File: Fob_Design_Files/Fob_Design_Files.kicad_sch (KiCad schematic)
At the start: 27 parts, among them IC2 TLV70030DDCT, U1 MAX16054AZT_T, U2 CC1101RGPR, U3 BU2032SM-JJ-GTR, U4 STM32C011F4Px, Y1 NX3225GA-26.000MHZ-EXS00A-CG0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

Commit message: Completed schematic
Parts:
- added J1: Conn_01x04_Pin, Connector_PinHeader_2.54mm:PinHeader_1x04_P2.54mm_Vertical, symbol Connector:Conn_01x04_Pin
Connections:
- net GND: now also J1.1 (Pin_1)
- net SWCLK: now also J1.2 (Pin_2)
- net SWDIO: now also J1.3 (Pin_3)
- net VDD: now also J1.4 (Pin_4)
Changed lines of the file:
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@@
 		)
 	)
+	(global_label "SWDIO"
+		(shape input)
+		(at 232.41 74.93 180)
+		(fields_autoplaced yes)
+		(effects
+			(font
+				(size 1.27 1.27)
+			)
+			(justify right)
+		)
+		(property "Intersheetrefs" "${INTERSHEET_REFS}"
+			(at 223.5586 74.93 0)
+			(effects
+				(font
+					(size 1.27 1.27)
+				)
+				(justify right)
+				(hide yes)
+			)
+		)
+	)
 	(global_label "RBIAS"
 		(shape input)
@@
 		)
 	)
+	(global_label "VDD"
+		(shape input)
+		(at 232.41 72.39 180)
+		(fields_autoplaced yes)
+		(effects
+			(font
+				(size 1.27 1.27)
+			)
+			(justify right)
+		)
+		(property "Intersheetrefs" "${INTERSHEET_REFS}"
+			(at 225.7962 72.39 0)
+			(effects
+				(font
+					(size 1.27 1.27)
+				)
+				(justify right)
+				(hide yes)
+			)
+		)
+	)
 	(global_label "SWDIO"
 		(shape input)
@@
 		)
 	)
+	(global_label "SWCLK"
+		(shape input)
+		(at 232.41 77.47 180)
+		(fields_autoplaced yes)
+		(effects
+			(font
+				(size 1.27 1.27)
+			)
+			(justify right)
+		)
+		(property "Intersheetrefs" "${INTERSHEET_REFS}"
+			(at 223.1958 77.47 0)
+			(effects
+				(font
+					(size 1.27 1.27)
+				)
+				(justify right)
+				(hide yes)
+			)
+		)
+	)
 	(symbol
 		(lib_id "SamacSys_Parts:BU2032SM-JJ-GTR")
@@
 	)
 	(symbol
+		(lib_id "Connector:Conn_01x04_Pin")
+		(at 237.49 77.47 180)
+		(unit 1)
+		(exclude_from_sim no)
+		(in_bom yes)
+		(on_board yes)
+		(dnp no)
+		(fields_autoplaced yes)
+		(property "Reference" "J1"
+			(at 238.76 74.9299 0)
+			(effects
+				(font
+					(size 1.27 1.27)
+				)
+				(justify right)
+			)
+		)
+		(property "Value" "Conn_01x04_Pin"
+			(at 238.76 77.4699 0)
+			(effects
+				(font
+					(size 1.27 1.27)
+				)
+				(justify right)
+			)
+		)
+		(property "Footprint" "Connector_PinHeader_2.54mm:PinHeader_1x04_P2.54mm_Vertical"
+			(at 237.49 77.47 0)
+			(effects
+				(font
+					(size 1.27 1.27)
+				)
+				(hide yes)
+			)
+		)
+		(property "Datasheet" "~"
+			(at 237.49 77.47 0)
+			(effects
+				(font
+					(size 1.27 1.27)
+				)
+				(hide yes)
+			)
+		)
+		(property "Description" "Generic connector, single row, 01x04, script generated"
+			(at 237.49 77.47 0)
+			(effects
+				(font
+					(size 1.27 1.27)
+				)
+				(hide yes)
+			)
+		)
+		(pin "1"
+		)
+		(pin "2"
+		)
+		(pin "4"
+		)
+		(pin "3"
+		)
+		(instances
+			(project ""
+				(path "/ad2bc408-bf54-4f88-a5fb-85c0e9c3efbd"
+					(reference "J1")
+					(unit 1)
+				)
+			)
+		)
+	)
+	(symbol
 		(lib_id "power:GND")
 		(at 224.79 44.45 0)
@@
 					(unit 1)
 				)
+			)
+		)
+	)
+	(symbol
+		(lib_id "power:GND")
+		(at 232.41 80.01 0)
+		(unit 1)
+		(exclude_from_sim no)
+		(in_bom yes)
+		(on_board yes)
+		(dnp no)
+		(fields_autoplaced yes)
+		(property "Reference" "#PWR027"
+			(at 232.41 86.36 0)
+			(effects
+				(font
+					(size 1.27 1.27)
+				)
+				(hide yes)
+			)
+		)
+		(property "Value" "GND"
+			(at 232.41 85.09 0)
+			(effects
+				(font
+					(size 1.27 1.27)
+				)
+			)
+		)
+		(property "Footprint" ""
+			(at 232.41 80.01 0)
+			(effects
+				(font
+					(size 1.27 1.27)
+				)
+				(hide yes)
+			)
+		)
+		(property "Datasheet" ""
+			(at 232.41 80.01 0)
+			(effects
+				(font
+					(size 1.27 1.27)
+				)
+				(hide yes)
+			)
+		)
+		(property "Description" "Power symbol creates a global label with name \"GND\" , ground"
+			(at 232.41 80.01 0)
+			(effects
+				(font
+					(size 1.27 1.27)
+				)
+				(hide yes)
+			)
+		)
+		(pin "1"
+		)
+		(instances
+			(project "Fob_Design_Files"
+				(path "/ad2bc408-bf54-4f88-a5fb-85c0e9c3efbd"
+					(reference "#PWR027")
+					(unit 1)
+				)

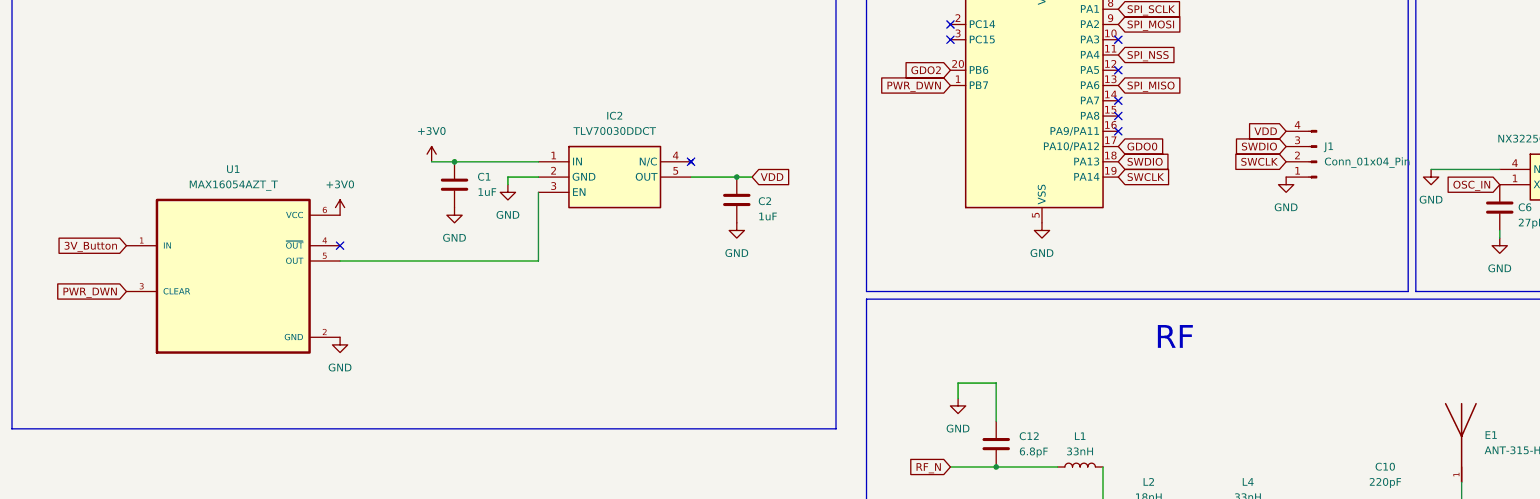
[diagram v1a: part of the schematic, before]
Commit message: Minor fob schematic changes
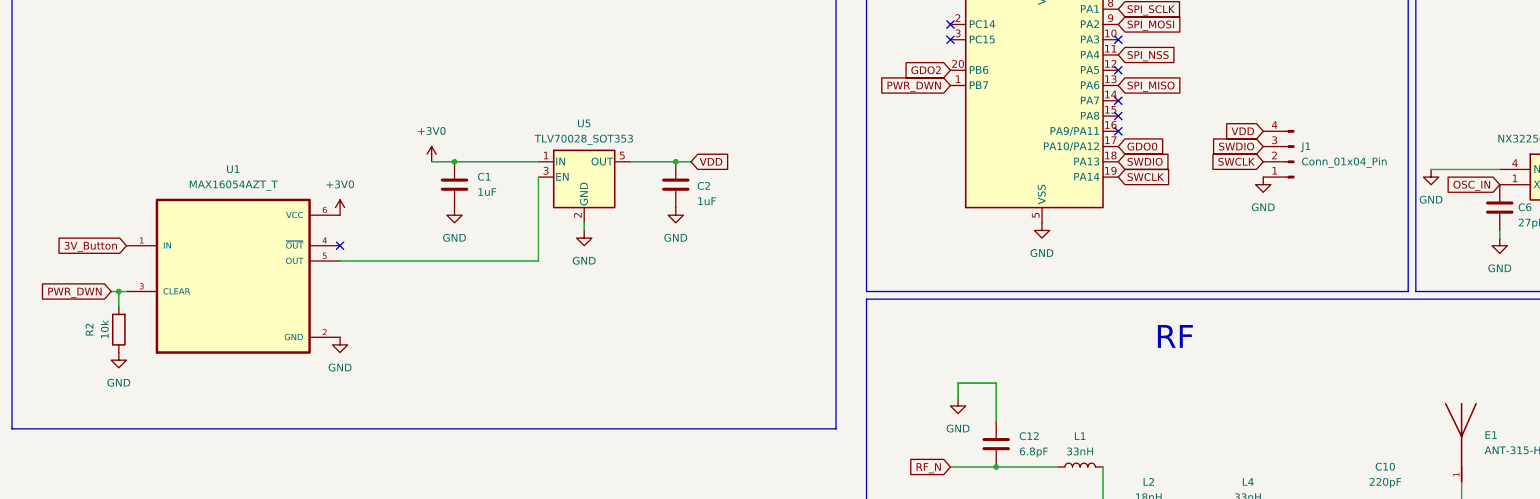
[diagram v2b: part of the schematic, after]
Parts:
- removed IC2: TLV70030DDCT, SamacSys_Parts:SOT95P280X110-5N, symbol SamacSys_Parts:TLV70030DDCT
- added R2: 10k, Resistor_SMD:R_0402_1005Metric, symbol Device:R
- added U5: TLV70028_SOT353, Package_TO_SOT_SMD:SOT-353_SC-70-5, symbol Regulator_Linear:TLV70028_SOT353
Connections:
- net +3V0: now also U5.1 (IN)
- net GND: now also R2.1, U5.2 (GND)
- net PWR_DWN: now also R2.2
- net VDD: now also U5.5 (OUT)
- net at U1.5 (OUT): now also U5.3 (EN)
- no-connect marks 12 -> 11
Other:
- moved on the sheet: C2, J1

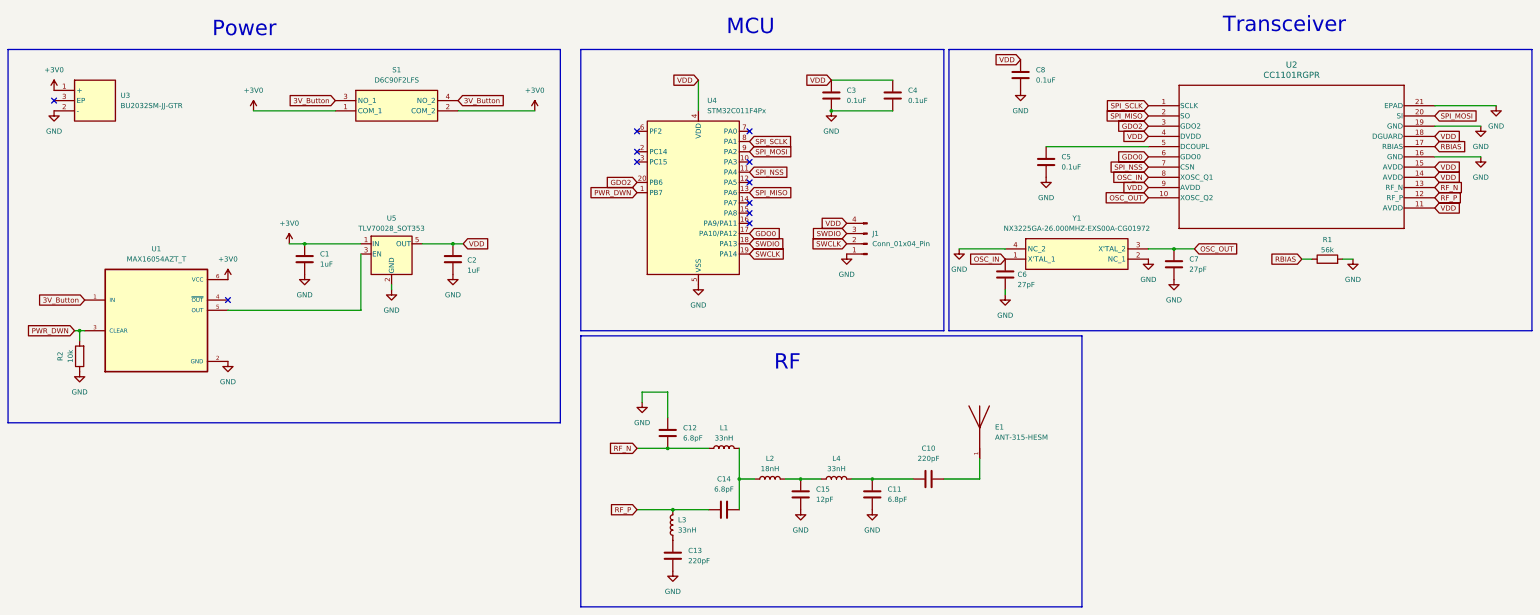
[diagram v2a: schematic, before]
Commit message: Added UART and indicator LEDs
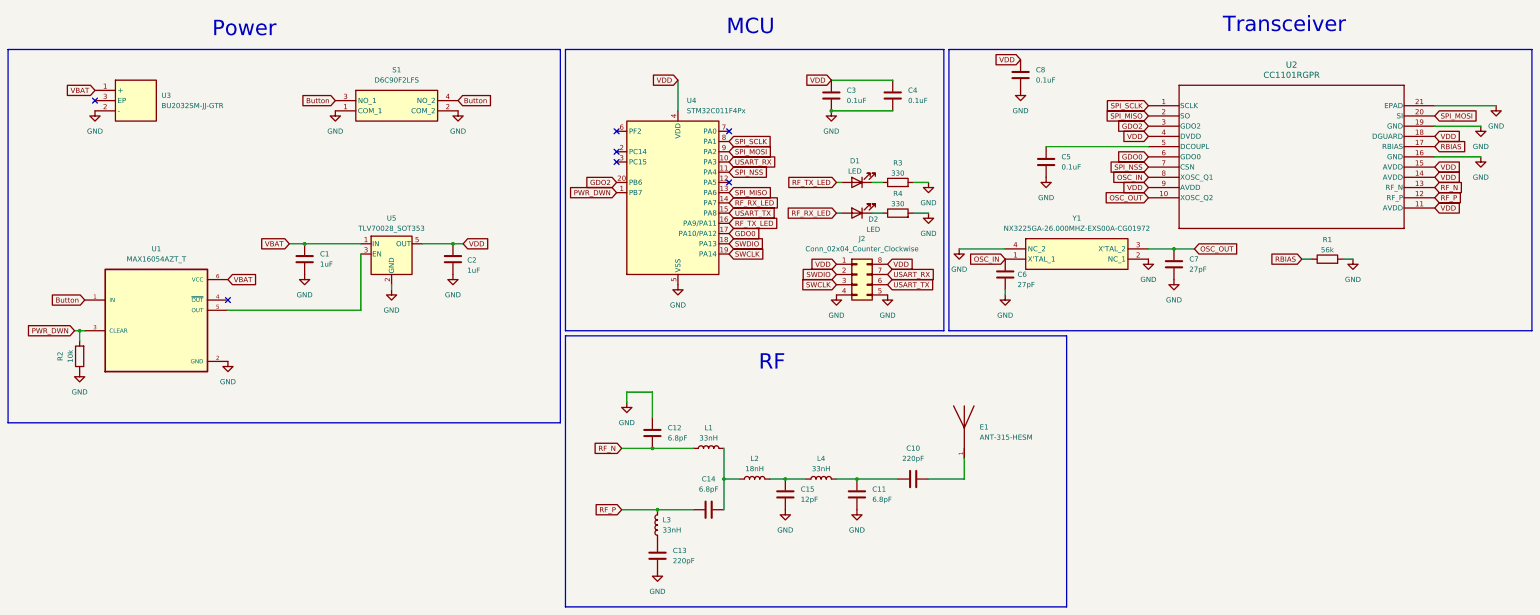
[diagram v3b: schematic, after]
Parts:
- removed J1: Conn_01x04_Pin, Connector_PinHeader_2.54mm:PinHeader_1x04_P2.54mm_Vertical, symbol Connector:Conn_01x04_Pin
- added D1, D2: LED, symbol Device:LED
- added J2: Conn_02x04_Counter_Clockwise, symbol Connector_Generic:Conn_02x04_Counter_Clockwise
- added R3, R4: 330, Resistor_SMD:R_0402_1005Metric, symbol Device:R
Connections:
- net GND: now also S1.1 (COM_1), S1.2 (COM_2), J2.4 (Pin_4), J2.5 (Pin_5), R3.2, R4.2
- net SWCLK: now also J2.3 (Pin_3)
- net SWDIO: now also J2.2 (Pin_2)
- net VDD: now also J2.1 (Pin_1), J2.8 (Pin_8)
- net USART_RX: now reaches U4.10 (PA3)
- net USART_RX: now also J2.7 (Pin_7)
- net RF_RX_LED: now reaches U4.14 (PA7)
- net RF_RX_LED: now also D2.2 (A)
- net USART_TX: now reaches U4.15 (PA8)
- net USART_TX: now also J2.6 (Pin_6)
- net RF_TX_LED: now reaches U4.16 (PA9/PA11)
- net RF_TX_LED: now also D1.2 (A)
- net +3V0 renamed VBAT
- net VBAT: no longer S1.1 (COM_1), S1.2 (COM_2)
- net 3V_Button renamed Button
- new net: D2.1 (K), R4.1
- new net: D1.1 (K), R3.1
- no-connect marks 11 -> 7
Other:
- moved on the sheet: C10, C11, C12, C13, C14, C15, E1, L1, L2, L3, L4, U3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

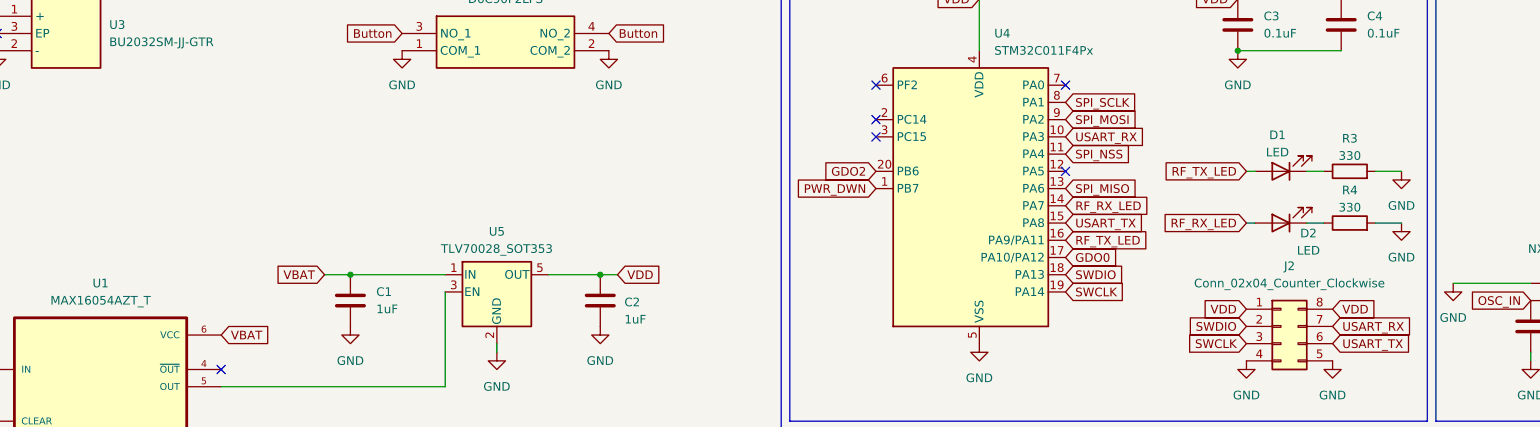
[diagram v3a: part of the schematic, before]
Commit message: Tolerance anaylsis LaTeX
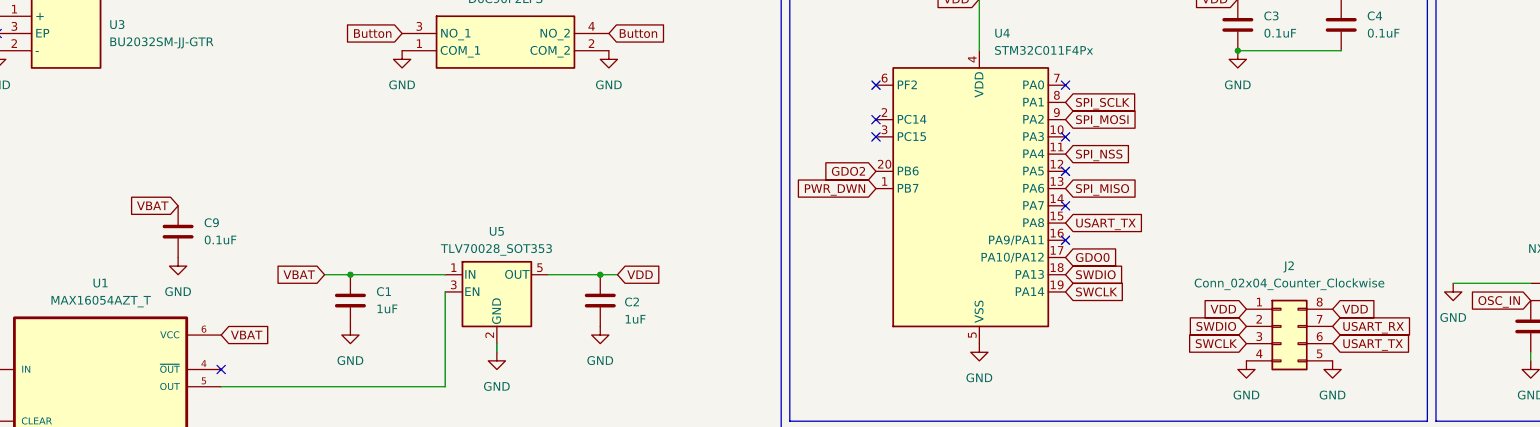
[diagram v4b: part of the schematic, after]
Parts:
- removed D1, D2: LED, symbol Device:LED
- removed R3, R4: 330, Resistor_SMD:R_0402_1005Metric, symbol Device:R
- added C9: 0.1uF, Capacitor_SMD:C_0603_1608Metric, symbol Device:C
- J2: footprint (none) -> Connector_PinSocket_2.54mm:PinSocket_2x04_P2.54mm_Vertical
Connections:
- net GND: now also C9.2
- net USART_RX: no longer U4.10 (PA3)
- net VBAT: now also C9.1
- net RF_RX_LED: no longer names the net of U4.14 (PA7)
- net RF_TX_LED: no longer names the net of U4.16 (PA9/PA11)
- no-connect marks 7 -> 10
